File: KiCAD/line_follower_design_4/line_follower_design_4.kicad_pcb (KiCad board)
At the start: 2 copper layers, 50 parts, among them M1 Motor Levi, M2 Motor Desni, Q1 Q_NPN_BCE, Q2 BSS138, Q3 BSS138, Q4 Q_PMOS_GDS, SW1 switch_psh, SW2 switch, U1 MCP1703A-5002/MB

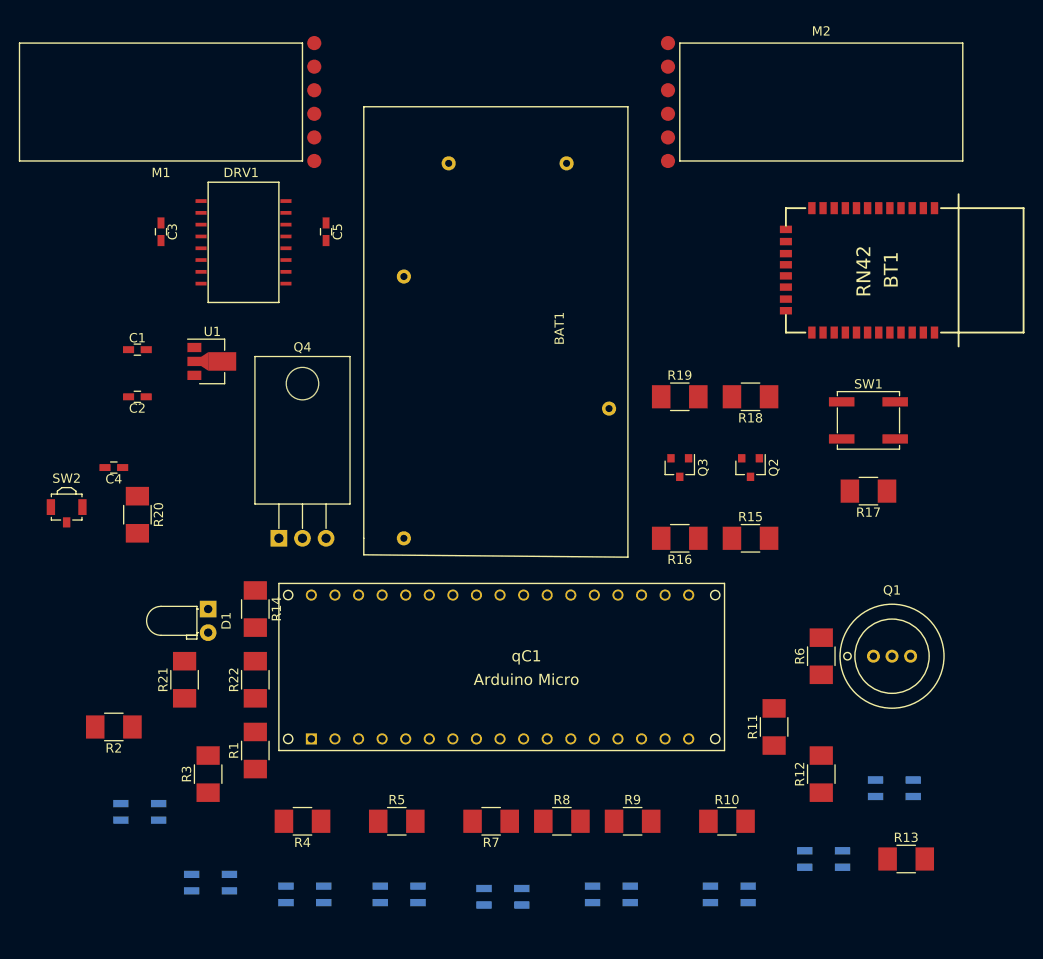
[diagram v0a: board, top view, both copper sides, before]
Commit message: line-follower-design-4 schematic update, pcb update
Library dependencies update, PCB components optimizations.
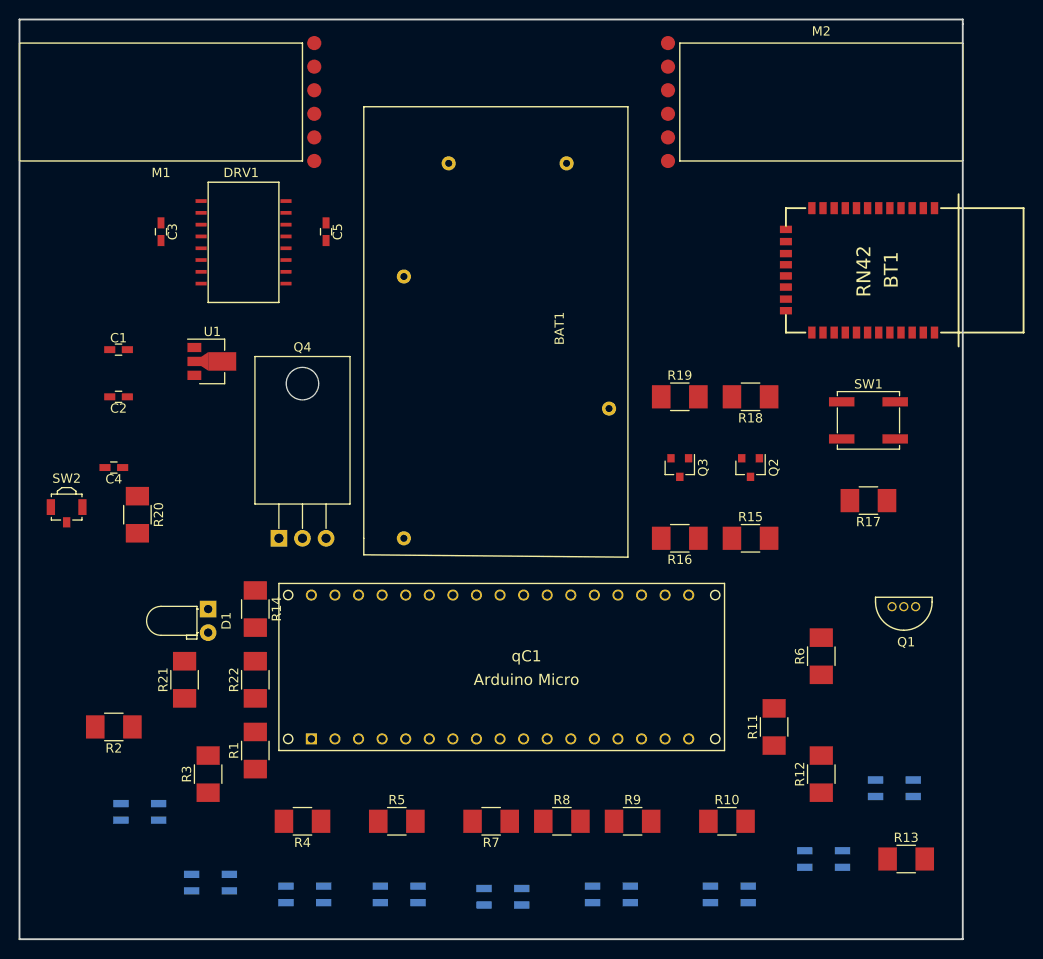
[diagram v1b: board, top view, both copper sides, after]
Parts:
- Q1: footprint Transistors_OldSowjetAera:OldSowjetaera_Transistor_Type-I_SmallPads -> BCE547B(T0-92):BCE547B(T0-92)
- moved Q1 2.27 mm to (-29.0, 119.9)
- moved C1 2.03 mm to (-111.3, 88.9)
- moved C2 2.03 mm to (-111.3, 94.0)
- moved R17 1.02 mm to (-30.5, 105.2)
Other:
- board outline added: 101.6 x 99.1 mm
- net class PWR: trace_width 0.5 -> 0.75; via_dia 0.6 -> 0.75
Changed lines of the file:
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@@
     (links 132)
     (no_connects 132)
-    (area -122.37 50.35 -13.469999 152.500001)
+    (area -122.020001 53.239999 -20.219999 152.500001)
     (thickness 1.6)
     (drawings 5)
@@
     (trace_min 0.2)
     (segment_width 0.2)
-    (edge_width 0.15)
+    (edge_width 0.2)
     (via_size 0.6)
     (via_drill 0.4)
@@
     (pad_to_mask_clearance 0.2)
     (aux_axis_origin 0 0)
-    (visible_elements 7FFFFFFF)
+    (visible_elements 7FFFF7FF)
     (pcbplotparams
       (layerselection 0x00030_80000001)
@@
   (net_class PWR ""
     (clearance 0.2)
-    (trace_width 0.5)
-    (via_dia 0.6)
+    (trace_width 0.75)
+    (via_dia 0.75)
     (via_drill 0.4)
     (uvia_dia 0.3)
@@
   )
   (module Capacitors_SMD:C_0603_HandSoldering (layer F.Cu)
-    (at -109.22 88.9)
+    (at -111.252 88.9)
     (descr "Capacitor SMD 0603, hand soldering")
     (tags "capacitor 0603")
@@
   )
   (module Capacitors_SMD:C_0603_HandSoldering (layer F.Cu)
-    (at -109.22 93.98 180)
+    (at -111.252 93.98 180)
     (descr "Capacitor SMD 0603, hand soldering")
     (tags "capacitor 0603")
@@
       (net 3 GND))
   )
-  (module Transistors_OldSowjetAera:OldSowjetaera_Transistor_Type-I_SmallPads (layer F.Cu)
-    (at -27.94 121.92)
-    (fp_text reference Q1 (at 0 -7.1) (layer F.SilkS)
-      (effects (font (size 1 1) (thickness 0.15)))
-    )
-    (fp_text value Q_NPN_BCE (at 0.1 7.6) (layer F.Fab)
-      (effects (font (size 1 1) (thickness 0.15)))
-    )
-    (fp_circle (center -4.8 0) (end -4.8 0.4) (layer F.SilkS) (width 0.15))
-    (fp_circle (center 0 0) (end 4 0) (layer F.SilkS) (width 0.15))
-    (fp_circle (center 0 0) (end 5.6 0) (layer F.SilkS) (width 0.15))
-    (pad 2 thru_hole circle (at 0 0) (size 1.4 1.4) (drill 0.8) (layers *.Cu *.Mask)
-      (net 48 "Net-(Q1-Pad2)"))
-    (pad 1 thru_hole circle (at -2 0) (size 1.4 1.4) (drill 0.8) (layers *.Cu *.Mask)
-      (net 49 "Net-(Q1-Pad1)"))
-    (pad 3 thru_hole circle (at 2 0) (size 1.4 1.4) (drill 0.8) (layers *.Cu *.Mask)
-      (net 3 GND))
-    (model Transistors_OldSowjetAera.3dshapes/OldSowjetaera_Transistor_Type-I_SmallPads.wrl
-      (at (xyz 0 0 0))
-      (scale (xyz 0.3937 0.3937 0.3937))
-      (rotate (xyz 0 0 0))
-    )
-  )
   (module TO_SOT_Packages_SMD:SOT-23 (layer F.Cu)
     (at -43.18 101.6 270)
@@
   )
   (module Resistors_SMD:R_1210_HandSoldering (layer F.Cu)
-    (at -30.48 104.14 180)
+    (at -30.48 105.156 180)
     (descr "Resistor SMD 1210, hand soldering")
     (tags "resistor 1210")
@@
       (net 18 "Net-(BT1-Pad31)"))
   )
-  (gr_line (start -20.32 53.848) (end -20.32 53.34) (angle 90) (layer B.Adhes) (width 0.2))
-  (gr_line (start -20.32 152.4) (end -20.32 53.848) (angle 90) (layer B.Adhes) (width 0.2))
-  (gr_line (start -121.92 152.4) (end -20.32 152.4) (angle 90) (layer B.Adhes) (width 0.2))
-  (gr_line (start -121.92 53.34) (end -121.92 152.4) (angle 90) (layer B.Adhes) (width 0.2))
-  (gr_line (start -20.32 53.34) (end -121.92 53.34) (angle 90) (layer B.Adhes) (width 0.2))
+  (module "BCE547B(T0-92):BCE547B(T0-92)" (layer F.Cu)
+    (at -28.956 119.888)
+    (fp_text reference Q1 (at 2.54 0.508) (layer F.SilkS)
+      (effects (font (size 1 1) (thickness 0.15)))
+    )
+    (fp_text value Q_NPN_BCE (at 2.286 -5.588) (layer F.Fab)
+      (effects (font (size 1 1) (thickness 0.15)))
+    )
+    (fp_line (start 5.334 -3.81) (end 5.334 -4.318) (layer F.SilkS) (width 0.15))
+    (fp_line (start -0.762 -3.81) (end -0.762 -4.318) (layer F.SilkS) (width 0.15))
+    (fp_line (start -0.762 -4.318) (end 5.334 -4.318) (layer F.SilkS) (width 0.15))
+    (fp_arc (start 2.286 -3.81) (end 2.286 -0.762) (angle 90) (layer F.SilkS) (width 0.15))
+    (fp_arc (start 2.286 -3.81) (end 5.334 -3.81) (angle 90) (layer F.SilkS) (width 0.15))
+    (pad 1 thru_hole circle (at 3.556 -3.302) (size 1 1) (drill 0.7) (layers *.Cu *.Mask)
+      (net 49 "Net-(Q1-Pad1)"))
+    (pad 2 thru_hole circle (at 2.286 -3.302) (size 1 1) (drill 0.7) (layers *.Cu *.Mask)
+      (net 48 "Net-(Q1-Pad2)"))
+    (pad 3 thru_hole circle (at 1.016 -3.302) (size 1 1) (drill 0.7) (layers *.Cu *.Mask)
+      (net 3 GND))
+  )
+  (gr_line (start -20.32 53.848) (end -20.32 53.34) (angle 90) (layer Edge.Cuts) (width 0.2))
+  (gr_line (start -20.32 152.4) (end -20.32 53.848) (angle 90) (layer Edge.Cuts) (width 0.2))
+  (gr_line (start -121.92 152.4) (end -20.32 152.4) (angle 90) (layer Edge.Cuts) (width 0.2))
+  (gr_line (start -121.92 53.34) (end -121.92 152.4) (angle 90) (layer Edge.Cuts) (width 0.2))
+  (gr_line (start -20.32 53.34) (end -121.92 53.34) (angle 90) (layer Edge.Cuts) (width 0.2))
   (zone (net 0) (net_name "") (layer F.Cu) (hatch edge 0.508)
     (connect_pads (clearance 0.508))
